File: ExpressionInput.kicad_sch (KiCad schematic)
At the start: 8 parts, among them J301 SJ2-25504B-SMT-TR

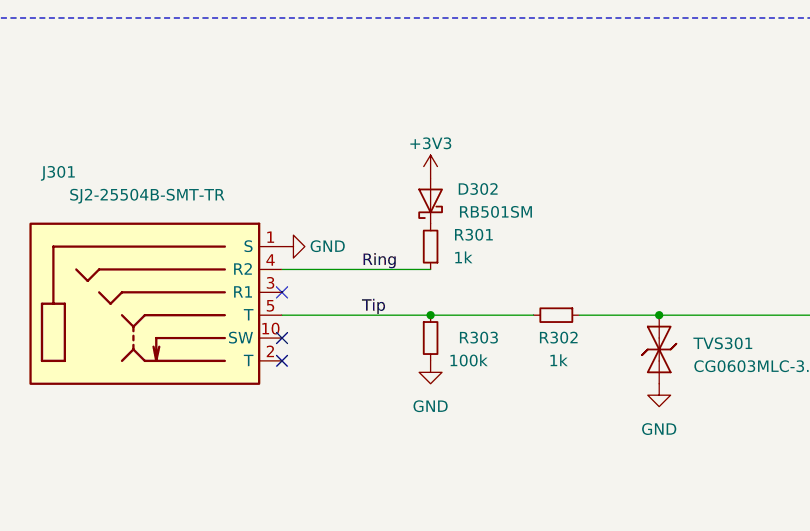
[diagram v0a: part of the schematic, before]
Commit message: Use the correct TRS pins
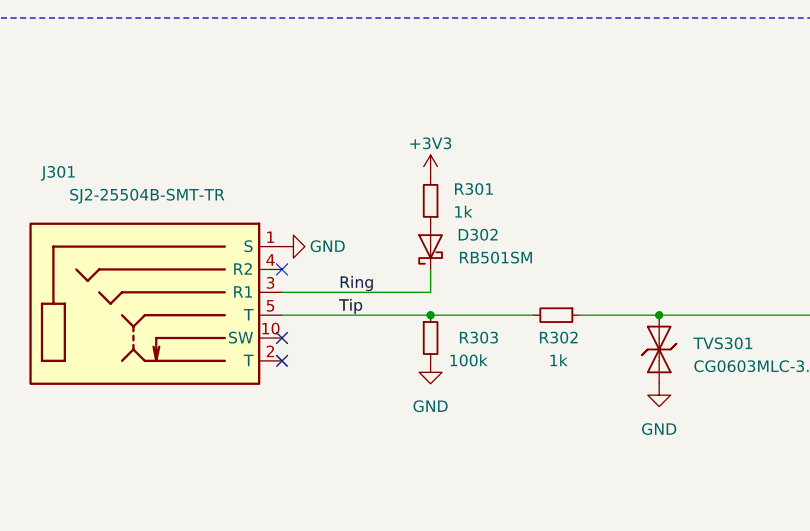
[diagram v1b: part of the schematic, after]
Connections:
- net +3V3: now also R301.2; no longer D302.2 (A)
- net Ring: now also D302.1 (K), J301.3 (R1); no longer J301.4 (R2), R301.1
- new net: D302.2 (A), R301.1
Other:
- moved on the sheet: D302, R301
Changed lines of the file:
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@@
 	)
 	(no_connect
-		(at 124.46 99.06)
+		(at 124.46 96.52)
 	)
 	(no_connect
 		(at 124.46 106.68)
+	)
+	(wire
+		(pts
+			(xy 140.97 96.52) (xy 140.97 99.06)
+		)
+		(stroke
+			(width 0)
+			(type default)
+		)
 	)
 	(polyline
@@
 		)
 	)
+	(wire
+		(pts
+			(xy 140.97 99.06) (xy 124.46 99.06)
+		)
+		(stroke
+			(width 0)
+			(type default)
+		)
+	)
 	(polyline
 		(pts
@@
 		)
 	)
+	(polyline
+		(pts
+			(xy 92.71 148.59) (xy 213.36 148.59)
+		)
+		(stroke
+			(width 0)
+			(type dash)
+		)
+	)
+	(polyline
+		(pts
+			(xy 213.36 148.59) (xy 213.36 68.58)
+		)
+		(stroke
+			(width 0)
+			(type dash)
+		)
+	)
 	(wire
 		(pts
-			(xy 124.46 96.52) (xy 140.97 96.52)
+			(xy 157.48 101.6) (xy 166.37 101.6)
 		)
 		(stroke
@@
 		)
 	)
-	(polyline
-		(pts
-			(xy 92.71 148.59) (xy 213.36 148.59)
-		)
-		(stroke
-			(width 0)
-			(type dash)
-		)
-	)
-	(polyline
-		(pts
-			(xy 213.36 148.59) (xy 213.36 68.58)
-		)
-		(stroke
-			(width 0)
-			(type dash)
-		)
-	)
 	(wire
 		(pts
-			(xy 157.48 101.6) (xy 166.37 101.6)
+			(xy 198.12 101.6) (xy 212.09 101.6)
 		)
 		(stroke
@@
 	(wire
 		(pts
-			(xy 198.12 101.6) (xy 212.09 101.6)
+			(xy 163.83 137.16) (xy 212.09 137.16)
 		)
 		(stroke
@@
 	(wire
 		(pts
-			(xy 163.83 137.16) (xy 212.09 137.16)
+			(xy 140.97 101.6) (xy 152.4 101.6)
 		)
 		(stroke
@@
 		)
 	)
-	(wire
-		(pts
-			(xy 140.97 101.6) (xy 152.4 101.6)
-		)
-		(stroke
-			(width 0)
-			(type default)
-		)
-	)
 	(label "Tip"
-		(at 133.35 101.6 0)
+		(at 130.81 101.6 0)
 		(fields_autoplaced yes)
 		(effects
@@
 	)
 	(label "Ring"
-		(at 133.35 96.52 0)
+		(at 130.81 99.06 0)
 		(fields_autoplaced yes)
 		(effects
@@
 	(symbol
 		(lib_id "Device:R_Small")
-		(at 140.97 93.98 180)
+		(at 140.97 88.9 180)
 		(unit 1)
 		(exclude_from_sim no)
@@
 		(dnp no)
 		(property "Reference" "R301"
-			(at 143.51 92.7101 0)
+			(at 143.51 87.6301 0)
 			(effects
 				(font
@@
 		)
 		(property "Value" "1k"
-			(at 143.51 95.25 0)
+			(at 143.51 90.17 0)
 			(effects
 				(font
@@
 		)
 		(property "Footprint" "Resistor_SMD:R_0603_1608Metric"
-			(at 140.97 93.98 0)
+			(at 140.97 88.9 0)
 			(effects
 				(font
@@
 		)
 		(property "Datasheet" "~"
-			(at 140.97 93.98 0)
-			(effects
-				(font
-					(size 1.27 1.27)
-				)
-				(hide yes)
-			)
-		)
-		(property "Description" ""
-			(at 140.97 93.98 0)
+			(at 140.97 88.9 0)
+			(effects
+				(font
+					(size 1.27 1.27)
+				)
+				(hide yes)
+			)
+		)
+		(property "Description" "Resistor, small symbol"
+			(at 140.97 88.9 0)
 			(effects
 				(font
@@
 			)
 		)
-		(property "Description" ""
+		(property "Description" "Resistor, small symbol"
 			(at 154.94 101.6 0)
 			(effects
@@
 			)
 		)
-		(property "Description" ""
+		(property "Description" "Power symbol creates a global label with name \"+3V3\""
 			(at 140.97 86.36 0)
 			(effects
@@
 			)
 		)
-		(property "Description" ""
+		(property "Description" "Power symbol creates a global label with name \"GND\" , ground"
 			(at 140.97 106.68 0)
 			(effects
@@
 			)
 		)
-		(property "Description" ""
+		(property "Description" "Power symbol creates a global label with name \"+5V\""
 			(at 163.83 134.62 0)
 			(effects
@@
 			)
 		)
-		(property "Description" ""
+		(property "Description" "Power symbol creates a global label with name \"GND\" , ground"
 			(at 198.12 106.68 0)
 			(effects
@@
 		(mirror y)
 		(unit 1)
-		(exclude_from_sim no)
+		(exclude_from_sim yes)
 		(in_bom yes)
 		(on_board yes)
@@
 		)
 		(property "Description" ""
-			(at 109.22 100.33 0)
-			(effects
-				(font
-					(size 1.27 1.27)
-				)
-				(hide yes)
-			)
-		)
-		(property "Sim.Enable" "0"
 			(at 109.22 100.33 0)
 			(effects
@@
 			)
 		)
-		(property "Description" ""
+		(property "Description" "Unpolarized capacitor, small symbol"
 			(at 198.12 104.14 0)
 			(effects
@@
 			)
 		)
-		(property "Description" ""
+		(property "Description" "Power symbol creates a global label with name \"GND\" , ground"
 			(at 163.83 139.7 0)
 			(effects
@@
 			)
 		)
-		(property "Description" ""
+		(property "Description" "Power symbol creates a global label with name \"GND\" , ground"
 			(at 166.37 109.22 0)
 			(effects
@@
 			)
 		)
-		(property "Description" ""
+		(property "Description" "Power symbol creates a global label with name \"GND\" , ground"
 			(at 124.46 93.98 0)
 			(effects
@@
 	(symbol
 		(lib_id "V2_Diode:RB501SM")
-		(at 140.97 88.9 90)
+		(at 140.97 93.98 90)
 		(unit 1)
 		(exclude_from_sim no)
@@
 		(dnp no)
 		(property "Reference" "D302"
-			(at 148.59 87.63 90)
+			(at 148.59 92.71 90)
 			(effects
 				(font
@@
 		)
 		(property "Value" "RB501SM"
-			(at 152.4 90.17 90)
+			(at 152.4 95.25 90)
 			(effects
 				(font
@@
 		)
 		(property "Footprint" "Diode_SMD:D_SOD-523"
-			(at 147.955 88.9 0)
+			(at 147.955 93.98 0)
 			(effects
 				(font
@@
 		)
 		(property "Datasheet" ""
-			(at 140.97 88.9 0)
+			(at 140.97 93.98 0)
 			(effects
 				(font
@@
 		)
 		(property "Description" ""
-			(at 140.97 88.9 0)
+			(at 140.97 93.98 0)
 			(effects
 				(font
@@
 			)
 		)
-		(property "Description" ""
+		(property "Description" "RGB LED with integrated controller"
 			(at 156.21 138.43 0)
 			(effects
@@
 			)
 		)
-		(property "Description" ""
+		(property "Description" "Resistor, small symbol"
 			(at 140.97 104.14 0)
 			(effects

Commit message: Udpate
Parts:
- R301: value 1k -> 33R
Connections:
- net Tip: now also J301.2 (T)
- no-connect marks 3 -> 2
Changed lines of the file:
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@@
 	(title_block
 		(title "Expression Input")
-		(date "2024-01-03")
-		(rev "2")
+		(date "2024-03-12")
+		(rev "4")
 		(company "Versio Duo")
 	)
@@
 	)
 	(junction
+		(at 127 101.6)
+		(diameter 0)
+		(color 0 0 0 0)
+	)
+	(junction
 		(at 140.97 101.6)
 		(diameter 0)
@@
 		(at 124.46 96.52)
 	)
-	(no_connect
-		(at 124.46 106.68)
+	(wire
+		(pts
+			(xy 127 106.68) (xy 127 101.6)
+		)
+		(stroke
+			(width 0)
+			(type default)
+		)
 	)
 	(wire
@@
 	(wire
 		(pts
+			(xy 124.46 106.68) (xy 127 106.68)
+		)
+		(stroke
+			(width 0)
+			(type default)
+		)
+	)
+	(wire
+		(pts
 			(xy 140.97 99.06) (xy 124.46 99.06)
 		)
@@
 	(wire
 		(pts
-			(xy 124.46 101.6) (xy 140.97 101.6)
+			(xy 124.46 101.6) (xy 127 101.6)
 		)
 		(stroke
@@
 			(width 0)
 			(type dash)
+		)
+	)
+	(wire
+		(pts
+			(xy 127 101.6) (xy 140.97 101.6)
+		)
+		(stroke
+			(width 0)
+			(type default)
 		)
 	)
@@
 			)
 		)
-		(property "Value" "1k"
+		(property "Value" "33R"
 			(at 143.51 90.17 0)
 			(effects
@@
 		(mirror y)
 		(unit 1)
-		(exclude_from_sim yes)
+		(exclude_from_sim no)
 		(in_bom yes)
 		(on_board yes)
@@
 			(at 109.22 100.33 0)
 			(effects
+				(font
+					(size 1.27 1.27)
+				)
+				(hide yes)
+			)
+		)
+		(property "Sim.Enable" "0"
+			(at 109.22 100.33 0)
+			(effects

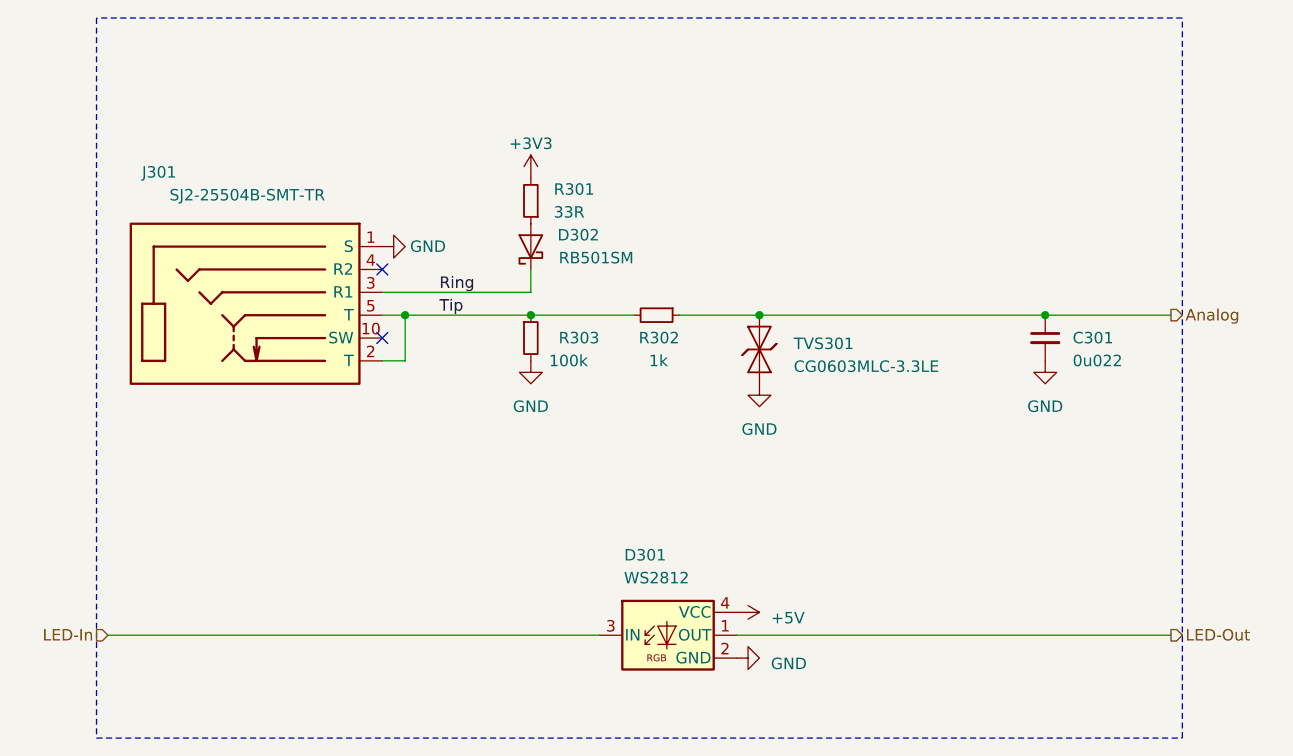
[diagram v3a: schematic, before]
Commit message: Replace TRS sockets
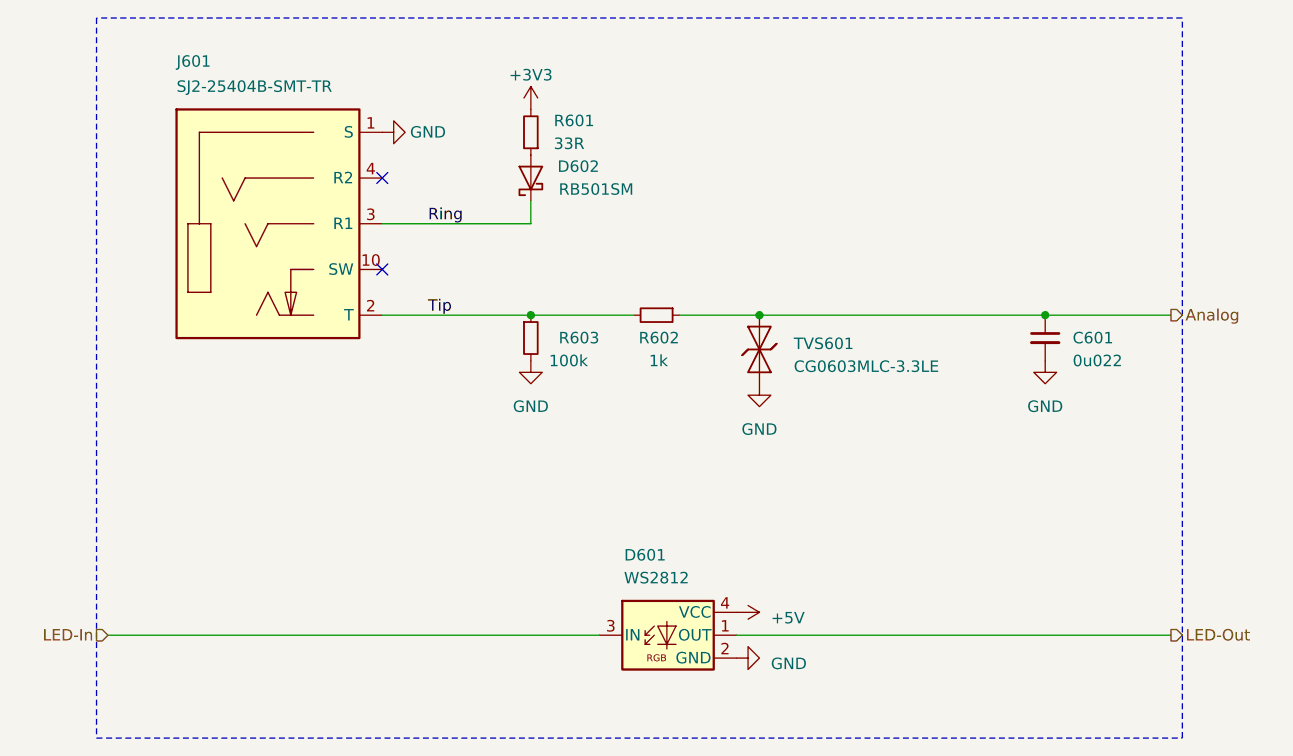
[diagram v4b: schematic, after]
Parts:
- J601: renamed from J301; value SJ2-25504B-SMT-TR -> SJ2-25404B-SMT-TR; footprint V2_Connector_Audio:CUI_SJ2-25504B-SMT-TR -> V2_Connector_Audio:CUI_SJ2-25404B-SMT-TR; symbol V2_Connector_Audio:SJ2-25504B-SMT-TR -> V2_Connector_Audio:SJ2-25404B-SMT-TR
- renumbered C301 to C601, D301 to D601, D302 to D602, R301 to R601, R302 to R602, R303 to R603, TVS301 to TVS601
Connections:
- net Tip: no longer J601.5 (T)
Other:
- moved on the sheet: D602, R601

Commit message: Convert to V2 Link
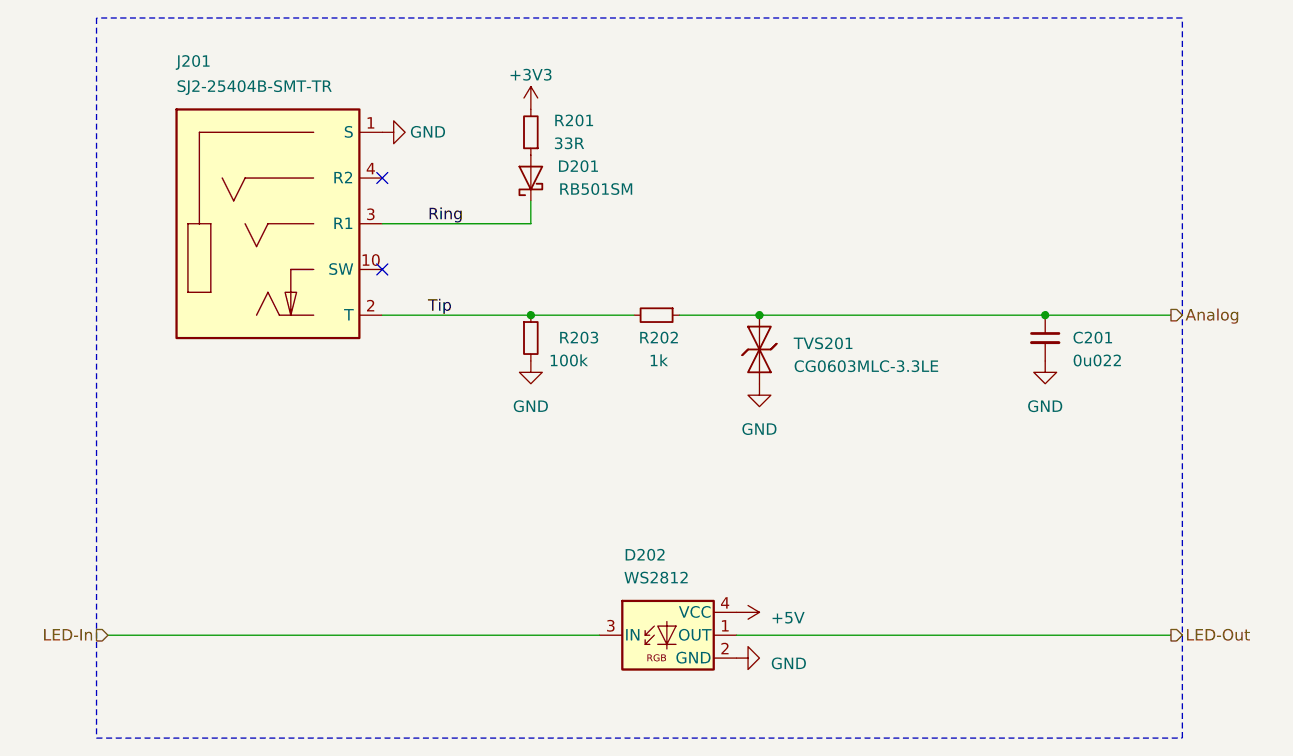
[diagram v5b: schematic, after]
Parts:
- renumbered C601 to C201, D602 to D201, D601 to D202, J601 to J201, R601 to R201, R602 to R202, R603 to R203, TVS601 to TVS201
